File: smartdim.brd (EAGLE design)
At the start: 38.1 x 10.2 mm, 7 parts, among them Q1 N-HEXFET-2D_SOT232-, U1 Tiny85-20-SMT

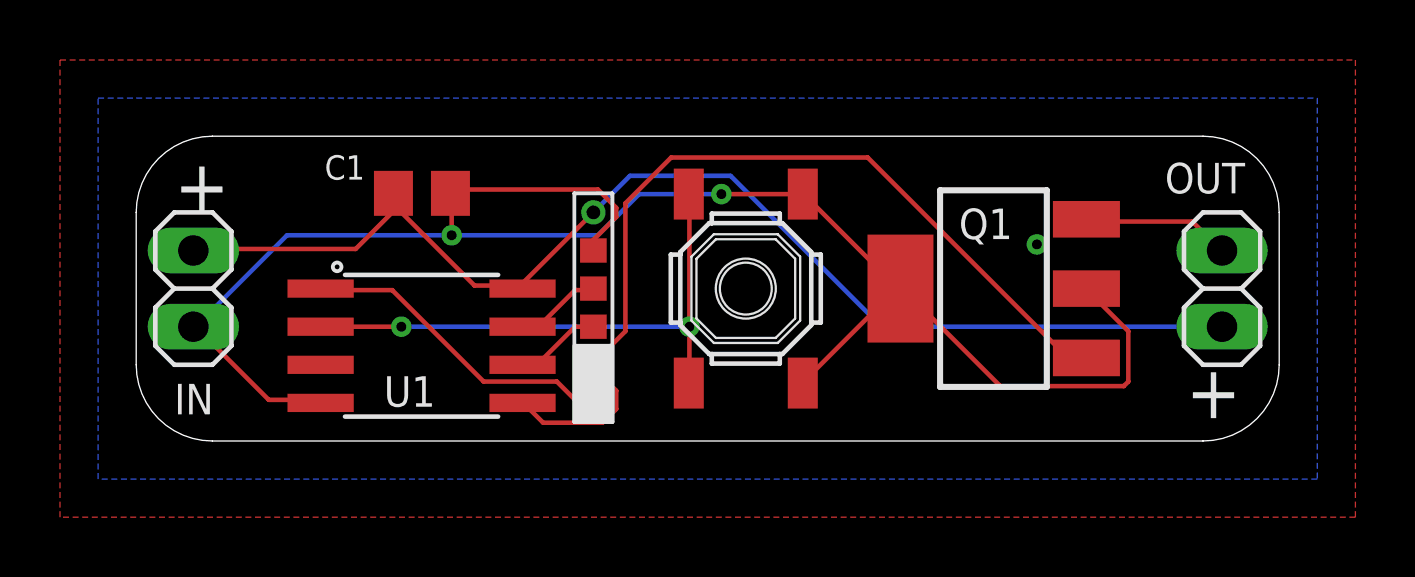
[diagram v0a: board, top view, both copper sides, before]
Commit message: osh-2: fix swapped MOSFET drain/source
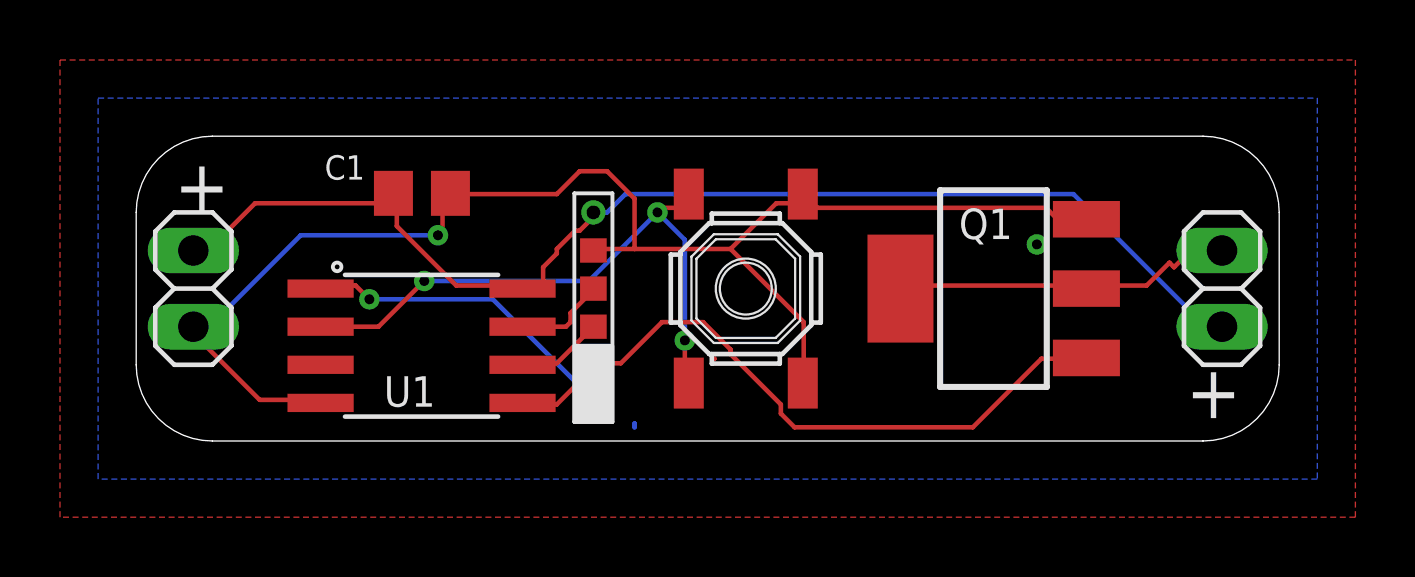
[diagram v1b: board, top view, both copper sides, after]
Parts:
- JP1: value (none) -> IN
- JP2: value (none) -> OUT
- SW1: value (none) -> USER
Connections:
- net GND: now also Q1.3; no longer Q1.2, Q1.4
- net PWM_VSS: now also Q1.2, Q1.4; no longer Q1.3
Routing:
- net GND: track 58.5 -> 48.1 mm, vias 2 -> 1
- net MOSI/PWM: track 30.0 -> 22.7 mm
- net PWM_VSS: track 4.97 -> 11.5 mm
- net USER_INPUT: track 18.6 -> 20.3 mm, vias 2 -> 3
- net NRES: track 10.7 -> 10.8 mm, vias 0 -> 1
- added copper zone on layer 1, net GND
- added copper zone on layer 16, net GND
- removed copper zone on layer 16, net N$1
- removed copper zone on layer 1, net N$2
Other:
- board text added: "smartdim osh-2"
- board text removed: "IN"
- board text removed: "OUT"
- board text removed: "smartdim osh-1"
